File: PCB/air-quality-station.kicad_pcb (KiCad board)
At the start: 4 copper layers, 63 parts, among them J1 USB_C_Receptacle_USB2.0_16P, J2 UART, J3 JST_PH_BATTERY, J4 SEN55, J5 I2C_1, J6 I2C_2, J9 E-Paper, Q1 Si1308EDL, U1 ESP32-C6-MINI-1/U, U2 SCD41-D-R2, U3 BMP280, U4 TLV73333PDBV, U5 BQ24075RGT, U6 USBLC6-2P6, U7 TLV73333PDBV, U8 TLV73333PDBV, Y1 32.768kHz

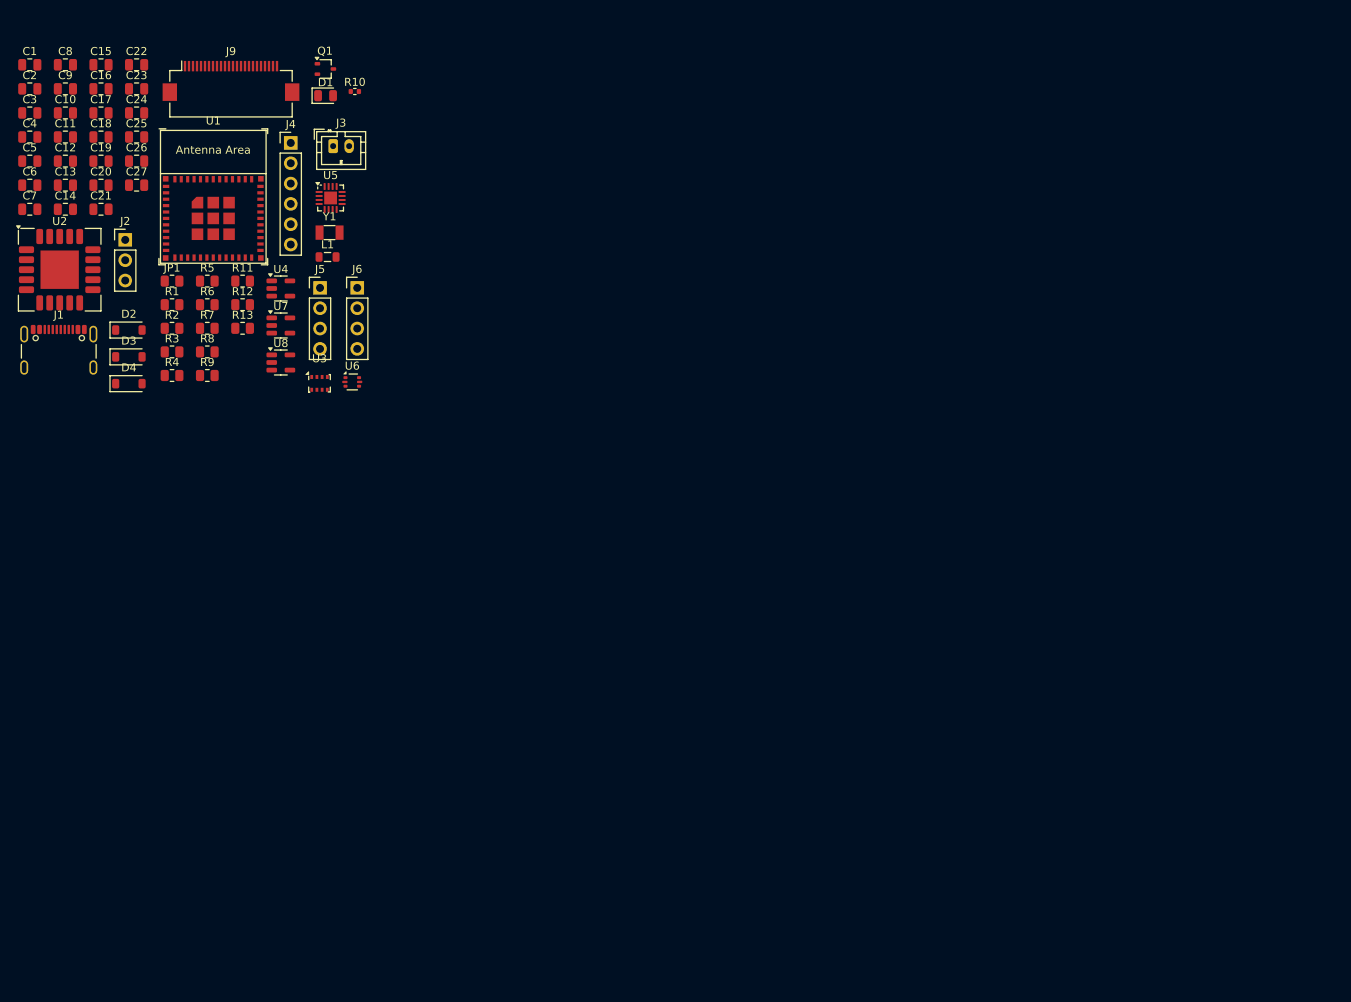
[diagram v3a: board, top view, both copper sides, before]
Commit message: First PCB layout, added mounting holes and PCB footprint
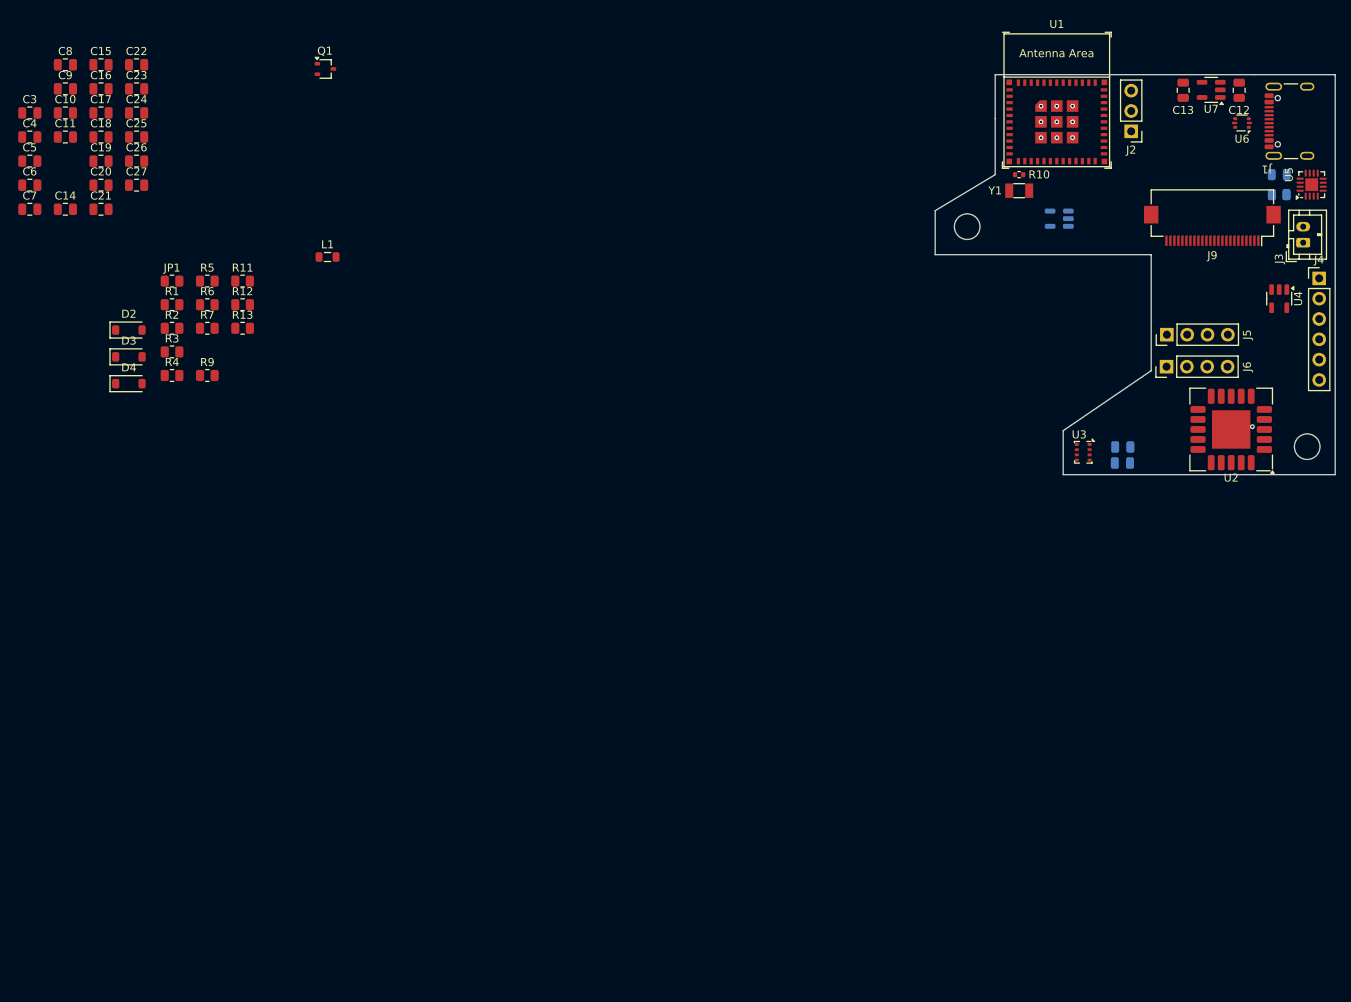
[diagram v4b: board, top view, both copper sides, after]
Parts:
- added H1: MountingHole, MountingHole:MountingHole_3.2mm_M3_DIN965, F.Cu at (146.5, 48.0)
- added H2: MountingHole, MountingHole:MountingHole_3.2mm_M3_DIN965, F.Cu at (189.0, 75.5)
- added PCB1: ~, PCBs:YAAQS_PCB, F.Cu at (161.0, 46.0)
- C1, C2, D1, R8, U8: moved to B.Cu
- moved J1 157.8 mm to (187.9, 34.8), turned to 90 degrees
- moved U2 147.8 mm to (179.5, 73.3), turned to 180 degrees
- moved C12 147.0 mm to (180.5, 30.9), turned to 90 degrees
- moved C1 145.4 mm to (165.9, 77.5), turned to 180 degrees
- moved C2 143.8 mm to (165.9, 75.5)
- moved C13 140.2 mm to (173.5, 30.9), turned to 90 degrees
- moved R8 135.4 mm to (185.5, 44.0)
- moved J4 129.7 mm to (190.5, 54.5)
- moved J2 126.5 mm to (167.0, 36.1), turned to 180 degrees
- moved U4 124.8 mm to (185.5, 57.0), turned to -90 degrees
- moved J9 124.0 mm to (177.2, 47.9), turned to 180 degrees
- moved U5 122.6 mm to (189.6, 42.8), turned to 90 degrees
- moved J3 121.9 mm to (188.5, 50.0), turned to 90 degrees
- moved U7 120.0 mm to (177.0, 30.9), turned to 180 degrees
- moved D1 119.6 mm to (185.5, 41.5), turned to 180 degrees
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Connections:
- J9 pad MP: (no net) -> GND
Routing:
- net GND: vias 0 -> 10
- added copper zone on In2.Cu, net +3V3_DISP
- added copper zone on In2.Cu, net +3V3_MCU
- added copper zone on In2.Cu, net +3V3_SEN
- added copper zone on In2.Cu, net +5V
- added copper zone on In1.Cu, net GND
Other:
- board outline added: 50 x 50 mm

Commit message: Updated schematic, finished PCB layout and routing
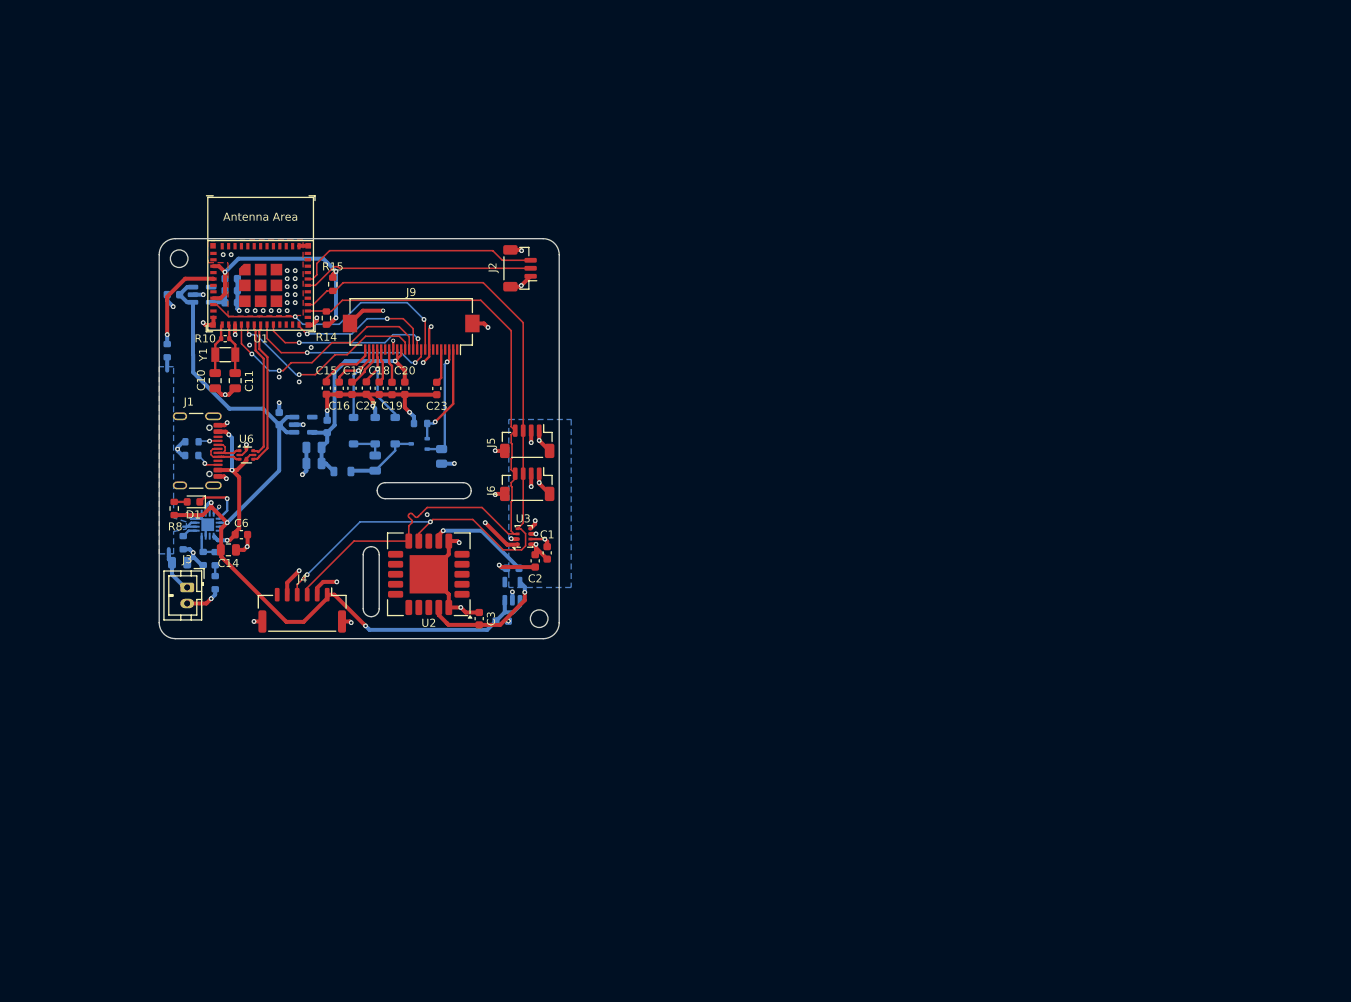
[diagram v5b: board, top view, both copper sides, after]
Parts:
- removed PCB1: ~, PCBs:YAAQS_PCB
- removed R1, R2, R3, R4: 10K, Resistor_SMD:R_0805_2012Metric
- added JP2: ~, Resistor_SMD:R_0603_1608Metric, B.Cu at (46.5, 63.5)
- added R14: 2.2K, Resistor_SMD:R_0603_1608Metric, F.Cu at (66.4, 59.4)
- added R15: 2.2K, Resistor_SMD:R_0603_1608Metric, F.Cu at (67.2, 55.2)
- C1, C2: footprint Capacitor_SMD:C_0805_2012Metric -> Capacitor_SMD:C_0603_1608Metric; moved to F.Cu
- C12, C13, C25, C26, C4, C5, C8, C9: footprint Capacitor_SMD:C_0805_2012Metric -> Capacitor_SMD:C_0603_1608Metric; moved to B.Cu
- C15, C16, C17, C18, C19, C20, C23, C27, C3, C6: footprint Capacitor_SMD:C_0805_2012Metric -> Capacitor_SMD:C_0603_1608Metric
- C21, C22, C24, C7, D2, D3, D4, L1, Q1, R13, U4, U5, U7: moved to B.Cu
- D1: footprint LED_SMD:LED_0805_2012Metric -> LED_SMD:LED_0603_1608Metric; moved to F.Cu
- H1, H2: footprint MountingHole:MountingHole_3.2mm_M3_DIN965 -> MountingHole:MountingHole_2.2mm_M2_ISO7380
- J2: footprint Connector_PinHeader_2.54mm:PinHeader_1x03_P2.54mm_Vertical -> Connector_JST:JST_SH_BM03B-SRSS-TB_1x03-1MP_P1.00mm_Vertical
- J4: footprint Connector_PinHeader_2.54mm:PinHeader_1x06_P2.54mm_Vertical -> Connector_JST:JST_GH_BM06B-GHS-TBT_1x06-1MP_P1.25mm_Vertical
- J5, J6: footprint Connector_PinHeader_2.54mm:PinHeader_1x04_P2.54mm_Vertical -> Connector_JST:JST_SH_BM04B-SRSS-TB_1x04-1MP_P1.00mm_Vertical
- JP1, R11, R5, R6, R7, R9: footprint Resistor_SMD:R_0805_2012Metric -> Resistor_SMD:R_0603_1608Metric; moved to B.Cu
- R12: value 2K -> 2.2K; footprint Resistor_SMD:R_0805_2012Metric -> Resistor_SMD:R_0603_1608Metric; moved to B.Cu
- R8: footprint Resistor_SMD:R_0805_2012Metric -> Resistor_SMD:R_0603_1608Metric; moved to F.Cu
- moved J3 146.0 mm to (49.0, 93.1), turned to -90 degrees
- moved J1 144.7 mm to (49.2, 76.0), turned to -90 degrees
- moved U5 144.4 mm to (51.6, 85.2), turned to 0 degrees
- moved R8 143.6 mm to (47.4, 83.2), turned to -90 degrees
- moved D1 141.7 mm to (49.8, 82.4)
- moved C12 135.7 mm to (47.3, 56.5), turned to 180 degrees
- moved J4 133.7 mm to (63.4, 96.0), turned to 180 degrees
- moved U6 131.2 mm to (56.4, 76.5), turned to 0 degrees
- moved U7 128.7 mm to (50.9, 56.5), turned to 0 degrees
- moved C13 121.9 mm to (54.5, 57.5), turned to 0 degrees
- moved U4 102.6 mm to (89.7, 93.6), turned to 90 degrees
- moved U2 101.9 mm to (79.2, 91.5)
- moved U1 101.6 mm to (58.2, 52.6)
- moved R10 101.3 mm to (53.8, 62.0)
- moved Y1 101.3 mm to (53.8, 64.0)
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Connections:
- J1 pad A6: Net-(J1-D+-PadA6) -> D+
- J1 pad A7: Net-(J1-D--PadA7) -> D-
- J1 pad B6: Net-(J1-D+-PadA6) -> D+
- J1 pad B7: Net-(J1-D--PadA7) -> D-
- U1 pad 5: unconnected-(U1-GPIO2/ADC1_CH2-Pad5) -> Net-(JP2-A)
- U6 pad 1: Net-(J1-D--PadA7) -> D-
- U6 pad 3: Net-(J1-D+-PadA6) -> D+
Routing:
- net GND: track 0.00 -> 168.9 mm, vias 10 -> 70
- net +5V: track 0.00 -> 110.3 mm, vias 0 -> 3
- net SCL: track 0.00 -> 96.9 mm, vias 0 -> 2
- net SDA: track 0.00 -> 89.9 mm
- net +3V3_SEN: track 0.00 -> 38.1 mm, vias 0 -> 7
- net +3V3_MCU: track 0.00 -> 35.0 mm, vias 0 -> 3
- net IO4_BUSY: track 0.00 -> 33.1 mm, vias 0 -> 2
- net UART_TX: track 0.00 -> 30.6 mm
- net +3V3_DISP: track 0.00 -> 30.5 mm, vias 0 -> 1
- net IO6_SCLK: track 0.00 -> 29.2 mm, vias 0 -> 2
- net UART_RX: track 0.00 -> 28.9 mm
- net IO7_SDI: track 0.00 -> 26.1 mm, vias 0 -> 2
- net D+: track 0.00 -> 23.6 mm
- net IO14_RES: track 0.00 -> 23.5 mm, vias 0 -> 2
- net +5V_BUS: track 0.00 -> 23.3 mm, vias 0 -> 3
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- added copper zone on B.Cu, net +3V3_SEN
- added copper zone on F.Cu, net GND
- added copper zone on In2.Cu, net GND
- added copper zone on B.Cu, net VBAT
- removed copper zone on In2.Cu, net +3V3_DISP
- removed copper zone on In2.Cu, net +3V3_MCU
- removed copper zone on In2.Cu, net +3V3_SEN
- removed copper zone on In2.Cu, net +5V
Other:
- outline, holes or cut-outs redrawn

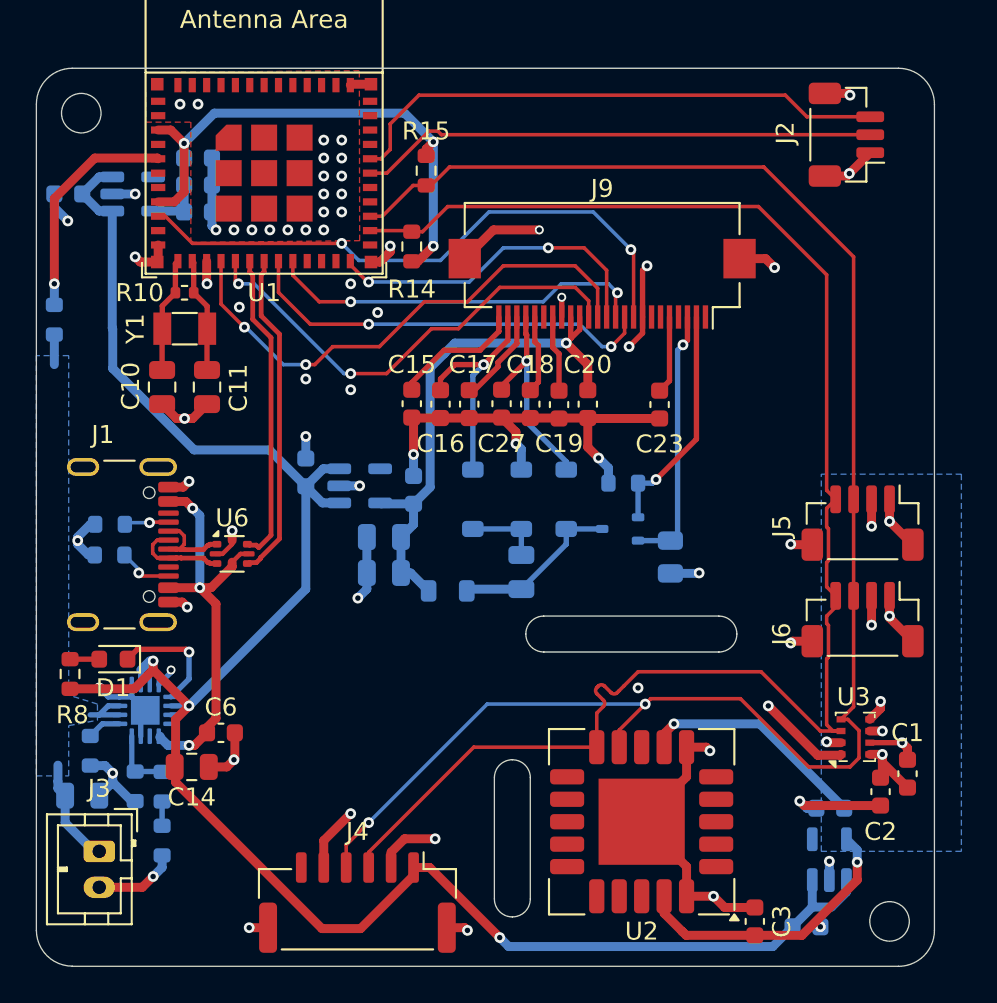
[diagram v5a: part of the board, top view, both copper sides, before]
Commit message: Drop battery support, add stitching vias and decooupling capacitors
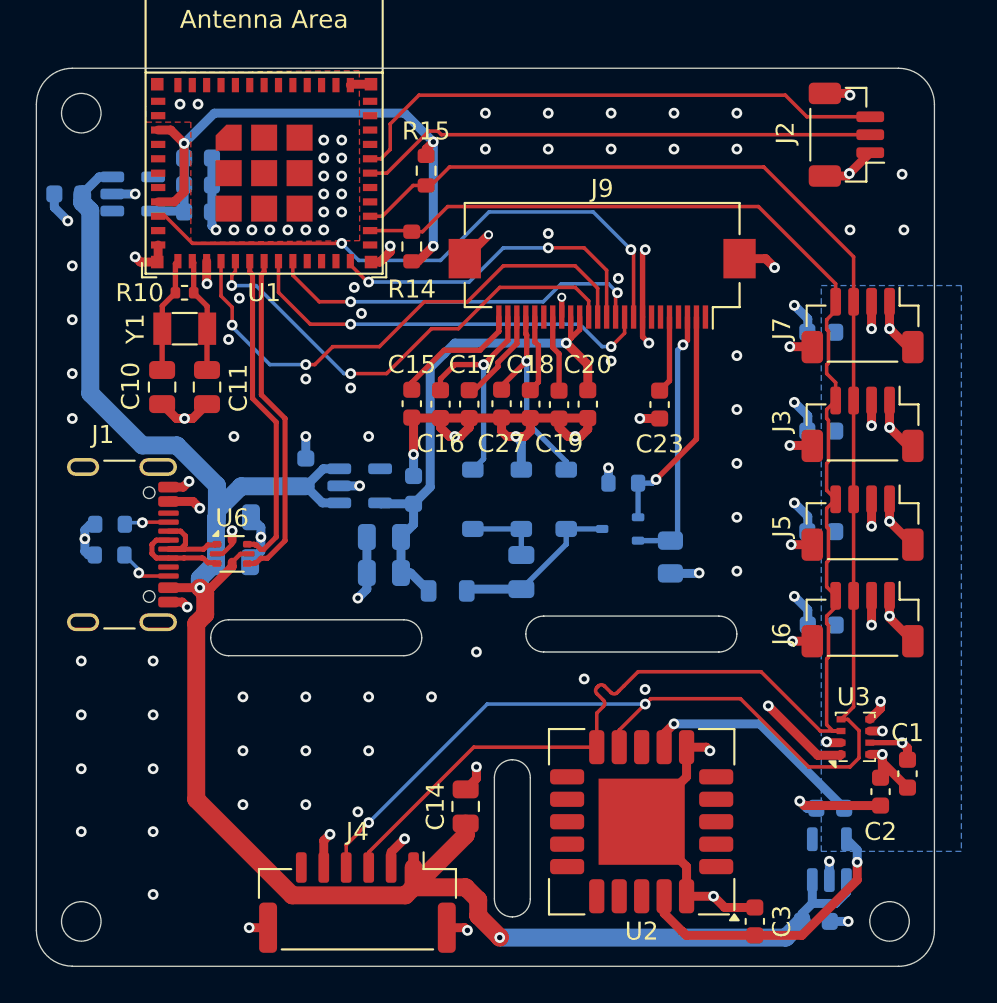
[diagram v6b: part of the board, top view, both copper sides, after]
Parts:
- removed D1: LED, LED_SMD:LED_0603_1608Metric
- removed JP1, JP2: ~, Resistor_SMD:R_0603_1608Metric
- removed R12: 2.2K, Resistor_SMD:R_0603_1608Metric
- removed R7, R8, R9: 10K, Resistor_SMD:R_0603_1608Metric
- removed U5: BQ24075RGT, Package_DFN_QFN:VQFN-16-1EP_3x3mm_P0.5mm_EP1.6x1.6mm
- added C28: 100nF, Capacitor_SMD:C_0603_1608Metric, B.Cu at (89.2, 80.5)
- added C29: 100nF, Capacitor_SMD:C_0603_1608Metric, B.Cu at (89.2, 75.3)
- added C30: 100nF, Capacitor_SMD:C_0603_1608Metric, B.Cu at (89.2, 69.7)
- added C31: 100nF, Capacitor_SMD:C_0603_1608Metric, B.Cu at (89.2, 64.2)
- added H3: MountingHole, MountingHole:MountingHole_2.2mm_M2_ISO7380, F.Cu at (48.0, 97.0)
- added J7: I2C_4, Connector_JST:JST_SH_BM04B-SRSS-TB_1x04-1MP_P1.00mm_Vertical, F.Cu at (91.5, 63.8)
- C6: value 1uF -> 4.7uF; footprint Capacitor_SMD:C_0603_1608Metric -> Capacitor_SMD:C_0805_2012Metric; moved to B.Cu
- J3: value JST_PH_BATTERY -> I2C_3; footprint Connector_JST:JST_PH_B2B-PH-K_1x02_P2.00mm_Vertical -> Connector_JST:JST_SH_BM04B-SRSS-TB_1x04-1MP_P1.00mm_Vertical
- moved J3 48.7 mm to (91.5, 69.3), turned to 180 degrees
- moved C7 15.5 mm to (56.5, 77.0)
- moved C14 15.4 mm to (69.4, 90.6), turned to 90 degrees
- moved C6 12.0 mm to (56.5, 74.5)
- moved C4 0.60 mm to (88.9, 97.0)
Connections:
- C14 pad 1: GND -> +5V
- C14 pad 2: +5V -> GND
- C6 pad 1: +5V_BUS -> +5V
- C7 pad 2: VBAT -> +5V
- J1 pad A4: +5V_BUS -> +5V
- J1 pad A9: +5V_BUS -> +5V
- J1 pad B4: +5V_BUS -> +5V
- J1 pad B9: +5V_BUS -> +5V
- J3 pad 1: VBAT -> GND
- J3 pad 2: GND -> +3V3_SEN
- U1 pad 5: Net-(JP2-A) -> unconnected-(U1-GPIO2/ADC1_CH2-Pad5)
- U6 pad 5: +5V_BUS -> +5V
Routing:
- net +5V_BUS: track 23.3 -> 0.00 mm, vias 3 -> 0
- net Net-(JP2-A): track 12.7 -> 0.00 mm, vias 1 -> 0
- net VBAT: track 10.6 -> 0.00 mm
- net Net-(D1-K): track 6.63 -> 0.00 mm, vias 1 -> 0
- net Net-(JP1-A): track 3.55 -> 0.00 mm
- net +3V3_SEN: track 38.1 -> 41.0 mm, vias 7 -> 9
- net +5V: track 110.3 -> 108.4 mm
- net Net-(U5-TS): track 1.90 -> 0.00 mm
- net Net-(D1-A): track 1.62 -> 0.00 mm
- net GND: track 168.9 -> 167.5 mm, vias 70 -> 127
- net Net-(JP1-B): track 1.35 -> 0.00 mm
- net SDA: track 89.9 -> 90.9 mm
- net D-: track 22.7 -> 23.5 mm
- net D+: track 23.6 -> 24.3 mm
- removed copper zone on B.Cu, net VBAT
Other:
- outline, holes or cut-outs redrawn
